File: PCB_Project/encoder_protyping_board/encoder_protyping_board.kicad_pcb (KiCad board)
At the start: 2 copper layers, 24.8 x 22.9 mm, 11 parts, among them J1 Conn_02x04_Counter_Clockwise, J2 Conn_01x02_Pin, J3 Conn_01x03_Pin

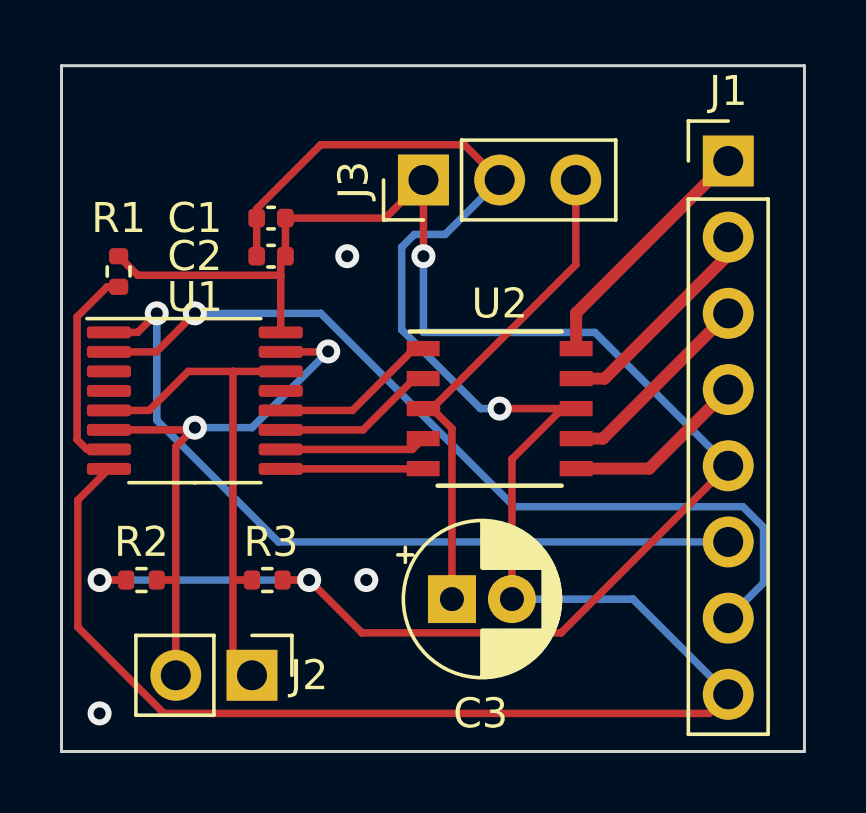
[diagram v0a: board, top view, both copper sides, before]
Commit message: fixed a trice width and did a bit of rerouting
0.4mm heading to the motor is all good but does not matter if the 12V power to the chip is not also 0.4mm wide
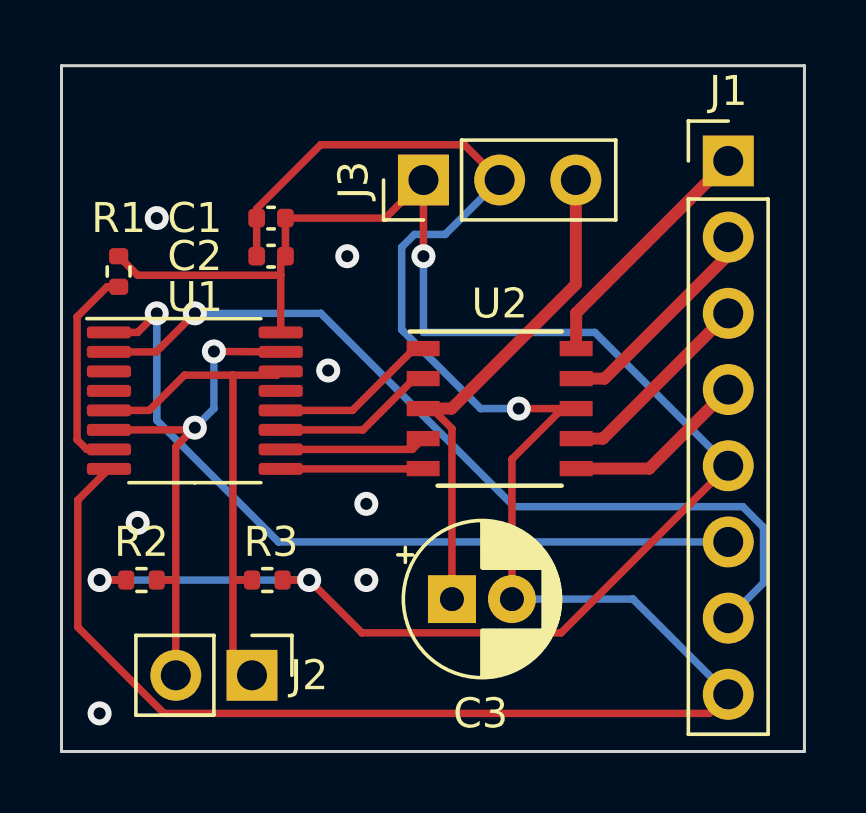
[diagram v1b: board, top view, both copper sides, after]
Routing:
- net I2C_SDA: track 19.1 -> 17.1 mm
- net +12V: track 17.0 -> 17.7 mm
- net GND: vias 4 -> 8
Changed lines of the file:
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@@
       (outputformat 1)
       (mirror false)
-      (drillshape 1)
+      (drillshape 0)
       (scaleselection 1)
       (outputdirectory "")
@@
   (segment (start 75.565 35.56) (end 76.2 34.925) (width 0.25) (layer "F.Cu") (net 2))
   (segment (start 55.5575 27.41) (end 54.52 28.4475) (width 0.25) (layer "F.Cu") (net 2))
+  (segment (start 69.215 25.4) (end 71.13 25.4) (width 0.25) (layer "F.Cu") (net 2))
   (segment (start 70.675 25.4) (end 71.13 25.4) (width 0.25) (layer "F.Cu") (net 2))
   (segment (start 68.989888 31.75) (end 68.989888 27.085112) (width 0.25) (layer "F.Cu") (net 2))
-  (segment (start 71.13 25.4) (end 68.58 25.4) (width 0.25) (layer "F.Cu") (net 2))
   (segment (start 68.989888 27.085112) (end 70.675 25.4) (width 0.25) (layer "F.Cu") (net 2))
   (segment (start 60.48 19.05) (end 60.48 20.32) (width 0.25) (layer "F.Cu") (net 2))
@@
   (segment (start 57.393299 35.56) (end 75.565 35.56) (width 0.25) (layer "F.Cu") (net 2))
   (via (at 64.135 31.115) (size 0.8) (drill 0.4) (layers "F.Cu" "B.Cu") (free) (net 2))
+  (via (at 69.215 25.4) (size 0.8) (drill 0.4) (layers "F.Cu" "B.Cu") (net 2))
   (via (at 55.245 35.56) (size 0.8) (drill 0.4) (layers "F.Cu" "B.Cu") (free) (net 2))
+  (via (at 56.515 29.21) (size 0.8) (drill 0.4) (layers "F.Cu" "B.Cu") (free) (net 2))
   (via (at 63.5 20.32) (size 0.8) (drill 0.4) (layers "F.Cu" "B.Cu") (free) (net 2))
-  (via (at 68.58 25.4) (size 0.8) (drill 0.4) (layers "F.Cu" "B.Cu") (net 2))
+  (via (at 62.865 24.13) (size 0.8) (drill 0.4) (layers "F.Cu" "B.Cu") (free) (net 2))
+  (via (at 57.15 19.05) (size 0.8) (drill 0.4) (layers "F.Cu" "B.Cu") (free) (net 2))
+  (via (at 64.135 28.575) (size 0.8) (drill 0.4) (layers "F.Cu" "B.Cu") (free) (net 2))
   (segment (start 65.315 22.771396) (end 67.943604 25.4) (width 0.25) (layer "B.Cu") (net 2))
   (segment (start 73.025 31.75) (end 68.989888 31.75) (width 0.25) (layer "B.Cu") (net 2))
-  (segment (start 67.943604 25.4) (end 68.58 25.4) (width 0.25) (layer "B.Cu") (net 2))
   (segment (start 65.315 20.019695) (end 65.315 22.771396) (width 0.25) (layer "B.Cu") (net 2))
+  (segment (start 67.943604 25.4) (end 69.215 25.4) (width 0.25) (layer "B.Cu") (net 2))
   (segment (start 65.739695 19.595) (end 65.315 20.019695) (width 0.25) (layer "B.Cu") (net 2))
   (segment (start 68.58 17.78) (end 66.765 19.595) (width 0.25) (layer "B.Cu") (net 2))
   (segment (start 76.2 34.925) (end 73.025 31.75) (width 0.25) (layer "B.Cu") (net 2))
   (segment (start 66.765 19.595) (end 65.739695 19.595) (width 0.25) (layer "B.Cu") (net 2))
+  (segment (start 71.12 17.78) (end 71.12 21.26) (width 0.4) (layer "F.Cu") (net 3))
   (segment (start 66.03 25.4) (end 66.325 25.4) (width 0.25) (layer "F.Cu") (net 3))
   (segment (start 66.989888 26.064888) (end 66.989888 31.75) (width 0.25) (layer "F.Cu") (net 3))
-  (segment (start 71.12 20.605) (end 71.12 17.78) (width 0.25) (layer "F.Cu") (net 3))
+  (segment (start 71.12 21.26) (end 66.98 25.4) (width 0.4) (layer "F.Cu") (net 3))
   (segment (start 66.485 25.4) (end 66.03 25.4) (width 0.25) (layer "F.Cu") (net 3))
+  (segment (start 66.98 25.4) (end 66.03 25.4) (width 0.4) (layer "F.Cu") (net 3))
   (segment (start 66.325 25.4) (end 66.989888 26.064888) (width 0.25) (layer "F.Cu") (net 3))
-  (segment (start 66.325 25.4) (end 71.12 20.605) (width 0.25) (layer "F.Cu") (net 3))
   (segment (start 71.13 23.4) (end 71.13 22.215) (width 0.4) (layer "F.Cu") (net 4))
   (segment (start 71.13 22.215) (end 76.2 17.145) (width 0.4) (layer "F.Cu") (net 4))
@@
   (segment (start 77.375 31.21) (end 76.2 32.385) (width 0.25) (layer "B.Cu") (net 9))
   (segment (start 69.065305 28.67) (end 76.686701 28.67) (width 0.25) (layer "B.Cu") (net 9))
+  (segment (start 58.073812 24.285) (end 59.69 24.285) (width 0.25) (layer "F.Cu") (net 10))
   (segment (start 59.69 33.655) (end 60.325 34.29) (width 0.25) (layer "F.Cu") (net 10))
-  (segment (start 59.69 24.16) (end 61.2825 24.16) (width 0.25) (layer "F.Cu") (net 10))
-  (segment (start 59.69 24.16) (end 59.69 31.115) (width 0.25) (layer "F.Cu") (net 10))
-  (segment (start 58.198812 24.16) (end 59.69 24.16) (width 0.25) (layer "F.Cu") (net 10))
+  (segment (start 61.1575 24.285) (end 61.2825 24.16) (width 0.25) (layer "F.Cu") (net 10))
+  (segment (start 59.69 24.285) (end 61.1575 24.285) (width 0.25) (layer "F.Cu") (net 10))
+  (segment (start 59.69 31.115) (end 59.69 24.285) (width 0.25) (layer "F.Cu") (net 10))
   (segment (start 59.69 31.115) (end 59.69 33.655) (width 0.25) (layer "F.Cu") (net 10))
-  (segment (start 56.898812 25.46) (end 58.198812 24.16) (width 0.25) (layer "F.Cu") (net 10))
+  (segment (start 56.898812 25.46) (end 58.073812 24.285) (width 0.25) (layer "F.Cu") (net 10))
   (segment (start 55.5575 25.46) (end 56.898812 25.46) (width 0.25) (layer "F.Cu") (net 10))
   (segment (start 60.325 31.115) (end 59.69 31.115) (width 0.25) (layer "F.Cu") (net 10))
+  (segment (start 61.2825 23.51) (end 59.055 23.495) (width 0.25) (layer "F.Cu") (net 11))
   (segment (start 58.42 26.035) (end 58.345 26.11) (width 0.25) (layer "F.Cu") (net 11))
   (segment (start 58.345 26.11) (end 55.5575 26.11) (width 0.25) (layer "F.Cu") (net 11))
-  (segment (start 61.2825 23.51) (end 62.85 23.51) (width 0.25) (layer "F.Cu") (net 11))
   (segment (start 58.42 26.035) (end 57.785 26.67) (width 0.25) (layer "F.Cu") (net 11))
   (segment (start 57.785 31.115) (end 57.785 34.29) (width 0.25) (layer "F.Cu") (net 11))
   (segment (start 57.785 26.67) (end 57.785 31.115) (width 0.25) (layer "F.Cu") (net 11))
+  (segment (start 59.055 23.495) (end 59.055 23.51) (width 0.25) (layer "F.Cu") (net 11))
   (segment (start 57.15 31.115) (end 57.785 31.115) (width 0.25) (layer "F.Cu") (net 11))
-  (segment (start 62.85 23.51) (end 62.865 23.495) (width 0.25) (layer "F.Cu") (net 11))
-  (via (at 62.865 23.495) (size 0.8) (drill 0.4) (layers "F.Cu" "B.Cu") (net 11))
+  (via (at 59.055 23.495) (size 0.8) (drill 0.4) (layers "F.Cu" "B.Cu") (net 11))
   (via (at 58.42 26.035) (size 0.8) (drill 0.4) (layers "F.Cu" "B.Cu") (net 11))
-  (segment (start 60.325 26.035) (end 58.42 26.035) (width 0.25) (layer "B.Cu") (net 11))
-  (segment (start 62.865 23.495) (end 60.325 26.035) (width 0.25) (layer "B.Cu") (net 11))
+  (segment (start 59.055 25.4) (end 58.42 26.035) (width 0.25) (layer "B.Cu") (net 11))
+  (segment (start 59.055 23.495) (end 59.055 25.4) (width 0.25) (layer "B.Cu") (net 11))
   (segment (start 54.495 26.434999) (end 54.495 22.34) (width 0.25) (layer "F.Cu") (net 12))
   (segment (start 54.495 22.34) (end 55.495 21.34) (width 0.25) (layer "F.Cu") (net 12))
@@
   (segment (start 63.675 25.46) (end 65.735 23.4) (width 0.25) (layer "F.Cu") (net 18))
   (segment (start 65.735 23.4) (end 66.03 23.4) (width 0.25) (layer "F.Cu") (net 18))
-  (zone (net 2) (net_name "GND") (layer "F.Cu") (hatch edge 0.5)
+  (zone (net 2) (net_name "GND") (layers "F&B.Cu") (hatch edge 0.5)
     (connect_pads (clearance 0.5))
     (min_thickness 0.25) (filled_areas_thickness no)
-    (fill yes (thermal_gap 0.5) (thermal_bridge_width 0.5))
-    (polygon
-      (pts
-        (xy 53.975 13.97)
-        (xy 78.74 13.97)
-        (xy 78.74 36.83)
-        (xy 53.975 36.83)
-      )
-    )
-  )
-  (zone (net 2) (net_name "GND") (layer "B.Cu") (hatch edge 0.5)
-    (priority 1)
-    (connect_pads (clearance 0.5))
-    (min_thickness 0.25) (filled_areas_thickness no)

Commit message: more vias on the ground plane and some rerouting
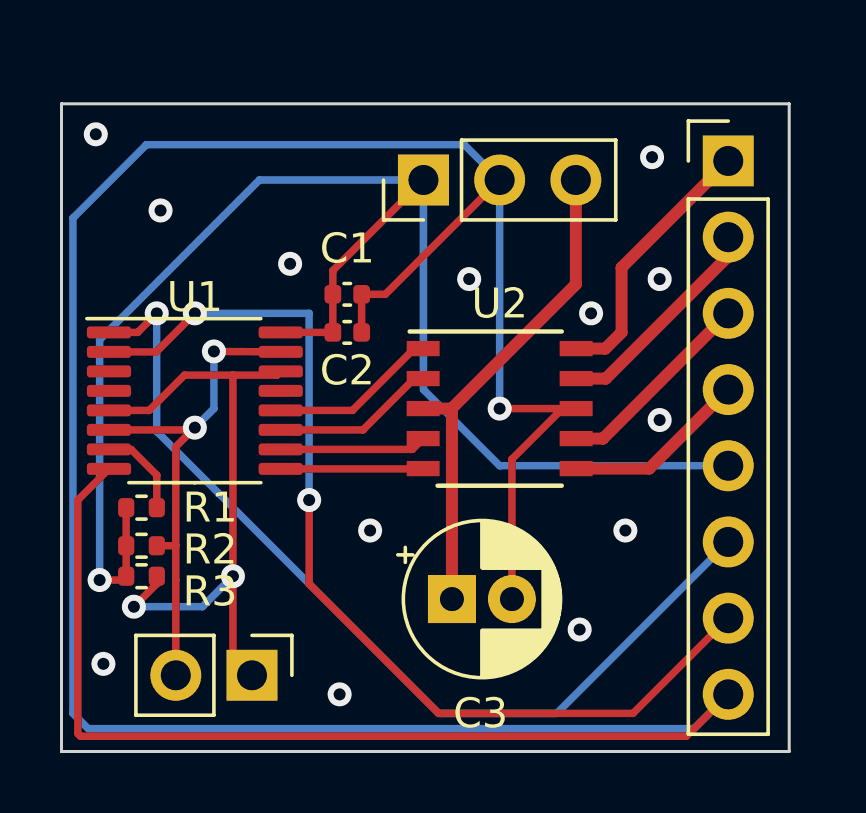
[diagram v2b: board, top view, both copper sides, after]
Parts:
- moved R1 7.91 mm to (56.6, 28.7), turned to 0 degrees
- moved R3 4.19 mm to (56.6, 31.0), turned to 180 degrees
- moved C1 3.59 mm to (63.5, 21.6), turned to 0 degrees
- moved C2 3.59 mm to (63.5, 22.9), turned to 0 degrees
- moved R2 1.14 mm to (56.6, 30.0)
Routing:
- net GND: track 69.8 -> 111.4 mm, vias 8 -> 14
- net +5V: track 57.5 -> 50.6 mm, vias 3 -> 1
- net Net-(J1-Pin_6): track 26.2 -> 31.1 mm
- net Net-(J1-Pin_7): track 28.8 -> 33.4 mm, vias 1 -> 2
- net I2C_SCL: track 17.2 -> 21.6 mm, vias 0 -> 2
- net Net-(U1-RESET): track 7.09 -> 3.03 mm
- net Net-(J1-Pin_1): track 8.36 -> 8.93 mm
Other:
- board size 24.8 x 22.9 mm -> 24.3 x 21.6 mm

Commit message: a better connected ground plane is a happy ground plane
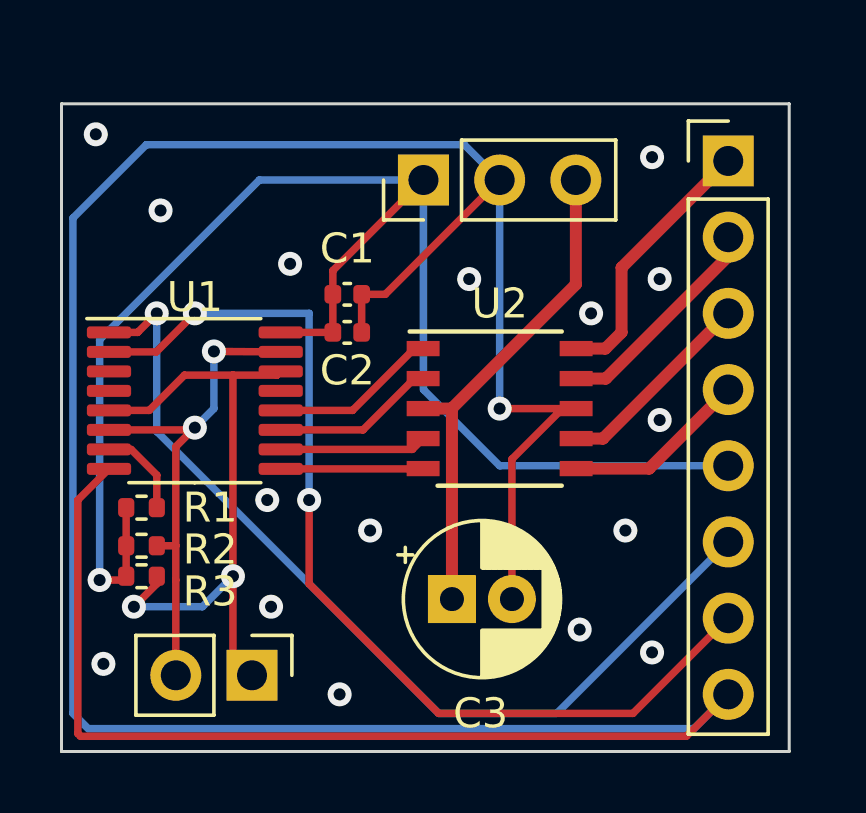
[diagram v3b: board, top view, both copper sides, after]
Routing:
- net GND: vias 14 -> 17
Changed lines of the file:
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@@
   (via (at 61.595 20.574) (size 0.8) (drill 0.4) (layers "F.Cu" "B.Cu") (free) (net 2))
   (via (at 72.771 29.464) (size 0.8) (drill 0.4) (layers "F.Cu" "B.Cu") (free) (net 2))
+  (via (at 60.833 28.448) (size 0.8) (drill 0.4) (layers "F.Cu" "B.Cu") (free) (net 2))
   (via (at 73.914 21.082) (size 0.8) (drill 0.4) (layers "F.Cu" "B.Cu") (free) (net 2))
+  (via (at 73.66 33.528) (size 0.8) (drill 0.4) (layers "F.Cu" "B.Cu") (free) (net 2))
   (via (at 55.118 16.256) (size 0.8) (drill 0.4) (layers "F.Cu" "B.Cu") (free) (net 2))
   (via (at 73.66 17.018) (size 0.8) (drill 0.4) (layers "F.Cu" "B.Cu") (free) (net 2))
+  (via (at 60.96 32.004) (size 0.8) (drill 0.4) (layers "F.Cu" "B.Cu") (free) (net 2))
   (via (at 63.246 34.925) (size 0.8) (drill 0.4) (layers "F.Cu" "B.Cu") (free) (net 2))
   (via (at 71.628 22.225) (size 0.8) (drill 0.4) (layers "F.Cu" "B.Cu") (free) (net 2))
@@
   (segment (start 56.515 22.86) (end 57.15 22.225) (width 0.25) (layer "F.Cu") (net 8))
   (via (at 57.15 22.225) (size 0.8) (drill 0.4) (layers "F.Cu" "B.Cu") (net 8))
+  (segment (start 57.15 26.162) (end 66.548 35.56) (width 0.25) (layer "B.Cu") (net 8))
+  (segment (start 66.548 35.56) (end 70.485 35.56) (width 0.25) (layer "B.Cu") (net 8))
   (segment (start 70.485 35.56) (end 76.2 29.845) (width 0.25) (layer "B.Cu") (net 8))
-  (segment (start 57.15 26.162) (end 66.548 35.56) (width 0.25) (layer "B.Cu") (net 8))
   (segment (start 57.15 22.225) (end 57.15 26.162) (width 0.25) (layer "B.Cu") (net 8))
-  (segment (start 66.548 35.56) (end 70.485 35.56) (width 0.25) (layer "B.Cu") (net 8))
   (segment (start 62.23 28.448) (end 62.23 31.242) (width 0.25) (layer "F.Cu") (net 9))
   (segment (start 57.135 23.51) (end 58.42 22.225) (width 0.25) (layer "F.Cu") (net 9))
@@
     (polygon
       (pts
-        (xy 53.975 15.24)
         (xy 78.232 15.24)
         (xy 78.232 36.83)
         (xy 53.975 36.83)
+        (xy 53.975 15.24)
       )
     )

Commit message: manual routing is fun
it is basically a puzzle
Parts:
- moved C1 3.77 mm to (64.3, 17.9)
- moved C2 3.77 mm to (64.3, 19.2)
- moved R1 2.19 mm to (58.6, 27.7)
- moved R2 2.19 mm to (58.6, 29.0)
- moved U1 2.19 mm to (60.4, 24.2)
- moved R3 2.19 mm to (58.6, 30.0)
- moved J2 1.98 mm to (62.2, 33.8)
- moved J3 1.55 mm to (67.5, 17.1)
- moved C3 0.40 mm to (67.1, 31.4)
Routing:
- net GND: track 111.4 -> 66.9 mm, vias 17 -> 23
- net I2C_SDA: track 17.1 -> 21.1 mm
- net Net-(J1-Pin_7): track 33.4 -> 30.6 mm
- net I2C_SCL: track 21.6 -> 19.1 mm, vias 2 -> 0
- net Net-(U1-OUT1): track 5.46 -> 3.09 mm
- net Net-(U1-OUT0): track 5.60 -> 3.23 mm
- net Net-(U1-OUT2): track 4.90 -> 3.04 mm
- net Net-(U1-OUT3): track 4.75 -> 3.20 mm
- net +12V: track 17.4 -> 18.3 mm
- net Net-(J1-Pin_6): track 31.1 -> 30.4 mm
- net +5V: track 50.6 -> 51.1 mm, vias 1 -> 2
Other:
- board size 24.3 x 21.6 mm -> 22 x 21.6 mm

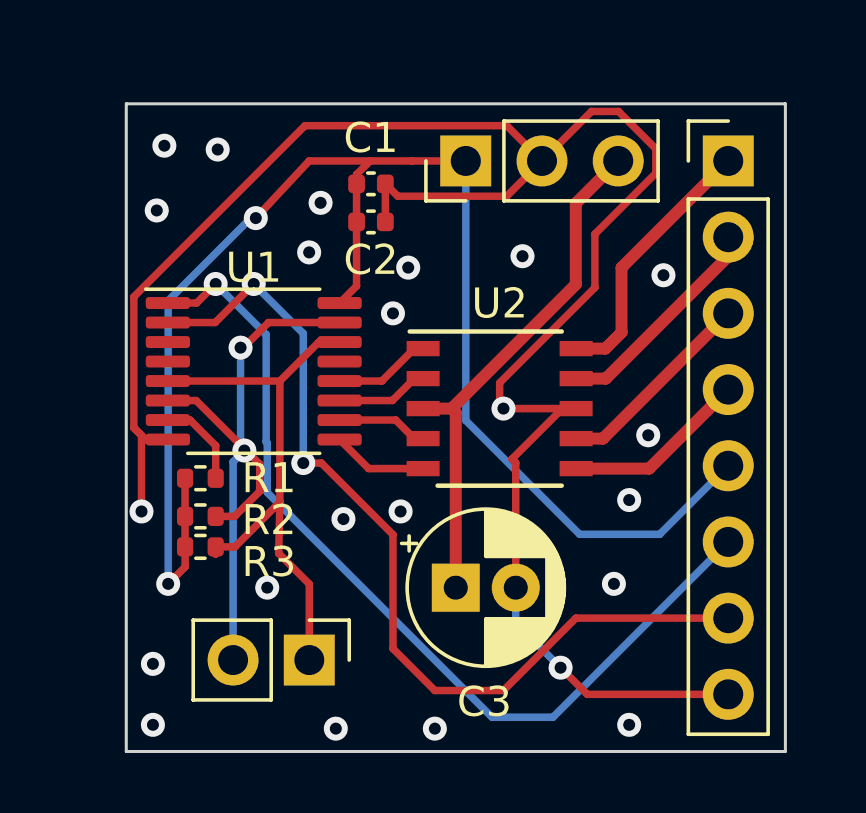
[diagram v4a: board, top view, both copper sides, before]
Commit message: added addresse jumpers
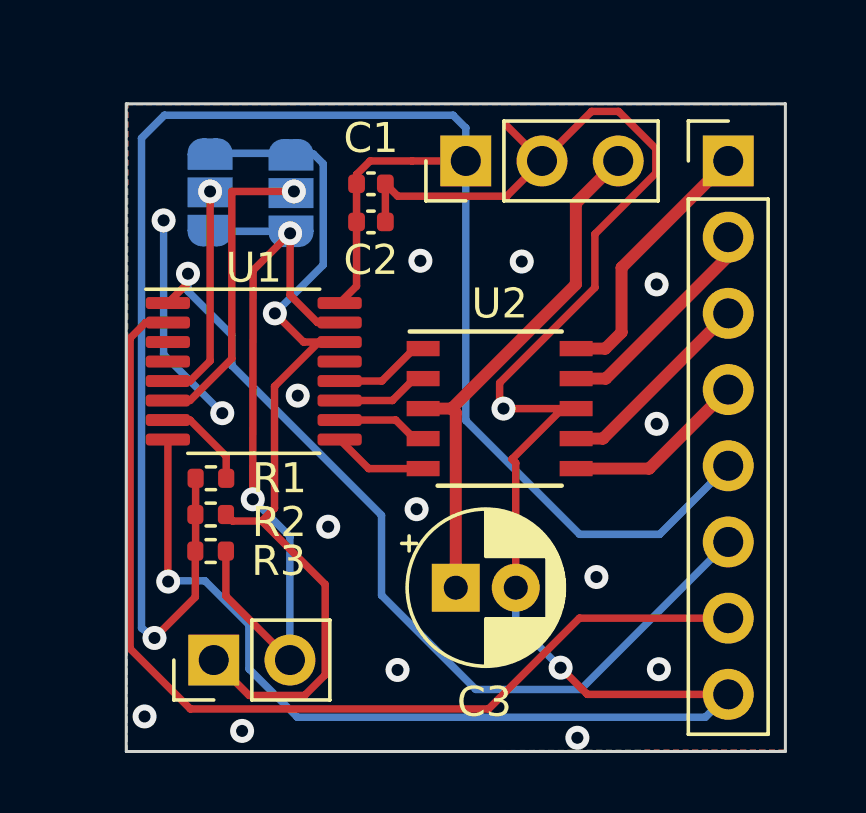
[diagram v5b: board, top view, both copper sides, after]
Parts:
- added JP1: SolderJumper_3_Open, Jumper:SolderJumper-3_P1.3mm_Open_RoundedPad1.0x1.5mm, B.Cu at (61.6, 18.2)
- added JP2: SolderJumper_3_Open, Jumper:SolderJumper-3_P1.3mm_Open_RoundedPad1.0x1.5mm_NumberLabels, B.Cu at (58.9, 18.2)
- moved J2 3.19 mm to (59.0, 33.8), turned to 90 degrees
- moved R3 1.21 mm to (58.9, 30.1)
- moved R2 1.13 mm to (58.9, 28.9)
- moved R1 0.35 mm to (59.0, 27.7)
- renumbered R3 to R2, R2 to R3
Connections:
- U1 pad 5: I2C_SCL -> Net-(JP2-C)
- U1 pad 6: I2C_SDA -> Net-(JP1-C)
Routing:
- net +5V: track 51.1 -> 64.2 mm, vias 2 -> 1
- net I2C_SCL: track 19.1 -> 31.4 mm, vias 0 -> 1
- net GND: track 66.9 -> 77.3 mm, vias 23 -> 18
- net Net-(JP1-C): track 0.00 -> 10.4 mm, vias 0 -> 1
- net Net-(JP2-C): track 0.00 -> 7.33 mm, vias 0 -> 1
- net I2C_SDA: track 21.1 -> 26.7 mm
- net Net-(J1-Pin_7): track 30.6 -> 33.9 mm, vias 2 -> 0
- net Net-(J1-Pin_6): track 30.4 -> 29.6 mm
